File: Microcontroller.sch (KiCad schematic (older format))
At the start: 41 parts, among them CN2 CONN_RCPT_USB2.0_MINI_B_SMD_R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, M1 2N7002BK, M2 2N7002BK, Q10 2N7002BK, U2 STM32L412R8T6, X1 ABM3B-16.000MHZ

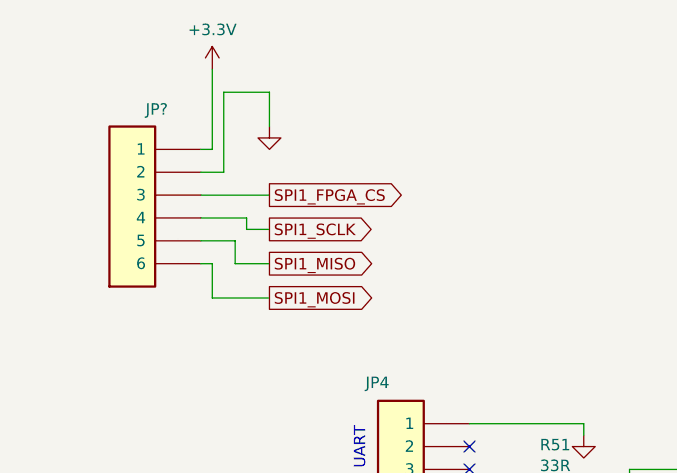
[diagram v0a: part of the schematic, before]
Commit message: Moved UART off FPGA bank 1, attached PB signals to FPGA
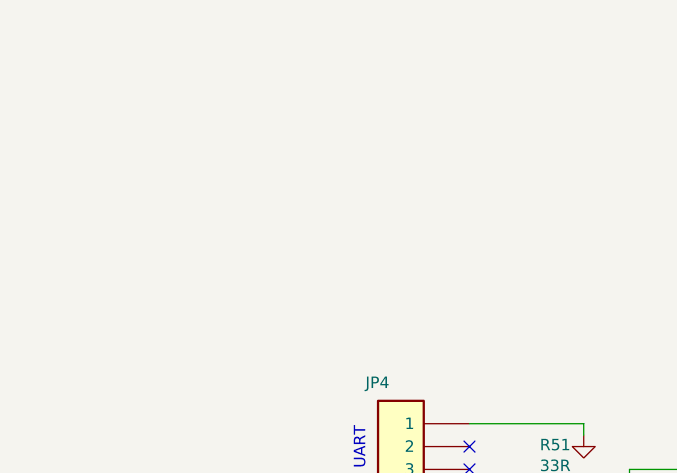
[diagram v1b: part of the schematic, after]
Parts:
- removed JP?: Pin_Header,_1x6-Way,_2.54mm_Pitch, symbol OpenVent:Pin_Header,_1x6-Way,_2.54mm_Pitch
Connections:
- wire segments 197 -> 181
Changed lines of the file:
@@
 Text Notes 8250 4150 0    50   ~ 0
 nRESET leftover from SWD,\nto be replaced with JTAG nRST\nsignal. LM 09/03/21
-$Comp
-L OpenVent:Pin_Header,_1x6-Way,_2.54mm_Pitch JP?
-U 1 1 6050B782
-P 1200 1700
-F 0 "JP?" H 1393 2375 50  0000 C CNN
-F 1 "Pin_Header,_1x6-Way,_2.54mm_Pitch" H 1400 2200 50  0001 C CNN
-F 2 "" H 1400 2200 50  0001 C CNN
-F 3 "" H 1400 2200 50  0001 C CNN
-	1    1200 1700
-	-1   0    0    -1
-$EndComp
-$Comp
-L OpenVent:+3.3V #PWR?
-U 1 1 6050E8FB
-P 1250 850
-F 0 "#PWR?" H 1250 700 50  0001 C CNN
-F 1 "+3.3V" H 1250 1023 50  0000 C CNN
-F 2 "" H 1250 850 50  0001 C CNN
-F 3 "" H 1250 850 50  0001 C CNN
-	1    1250 850
-	1    0    0    -1
-$EndComp
-$Comp
-L OpenVent:GND #PWR?
-U 1 1 6050F327
-P 1500 1100
-F 0 "#PWR?" H 1500 850 50  0001 C CNN
-F 1 "GND" H 1500 950 50  0001 C CNN
-F 2 "" H 1500 1100 50  0001 C CNN
-F 3 "" H 1500 1100 50  0001 C CNN
-	1    1500 1100
-	1    0    0    -1
-$EndComp
-Text GLabel 1500 1400 2    50   Output ~ 0
-SPI1_FPGA_CS
-Text GLabel 1500 1700 2    50   Output ~ 0
-SPI1_MISO
-Text GLabel 1500 1850 2    50   Output ~ 0
-SPI1_MOSI
-Text GLabel 1500 1550 2    50   Output ~ 0
-SPI1_SCLK
-Wire Wire Line
-	1200 1200 1250 1200
-Wire Wire Line
-	1250 1200 1250 850
-Wire Wire Line
-	1200 1300 1300 1300
-Wire Wire Line
-	1300 1300 1300 950
-Wire Wire Line
-	1300 950  1500 950
-Wire Wire Line
-	1500 950  1500 1100
-Wire Wire Line
-	1200 1400 1500 1400
-Wire Wire Line
-	1200 1500 1400 1500
-Wire Wire Line
-	1400 1500 1400 1550
-Wire Wire Line
-	1400 1550 1500 1550
-Wire Wire Line
-	1200 1600 1350 1600
-Wire Wire Line
-	1350 1600 1350 1700
-Wire Wire Line
-	1350 1700 1500 1700
-Wire Wire Line
-	1200 1700 1250 1700
-Wire Wire Line
-	1250 1700 1250 1850
-Wire Wire Line
-	1250 1850 1500 1850
 $EndSCHEMATC

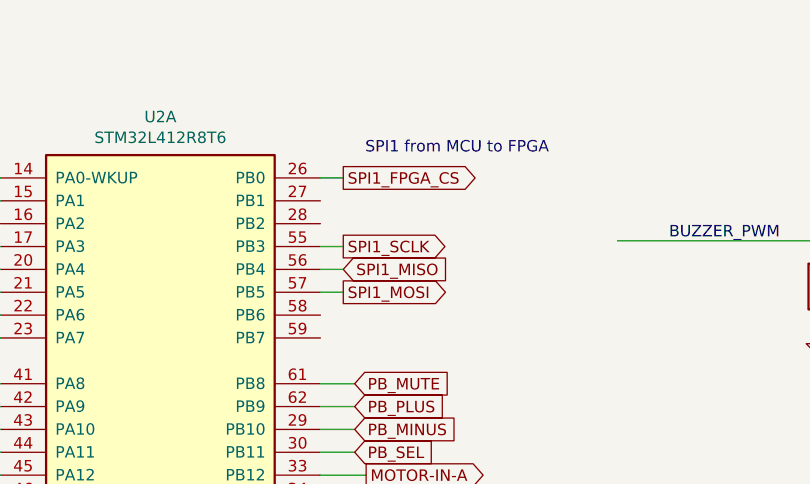
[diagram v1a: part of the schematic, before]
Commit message: Added FPGA_READY interrupt signal from FPGA to MCU
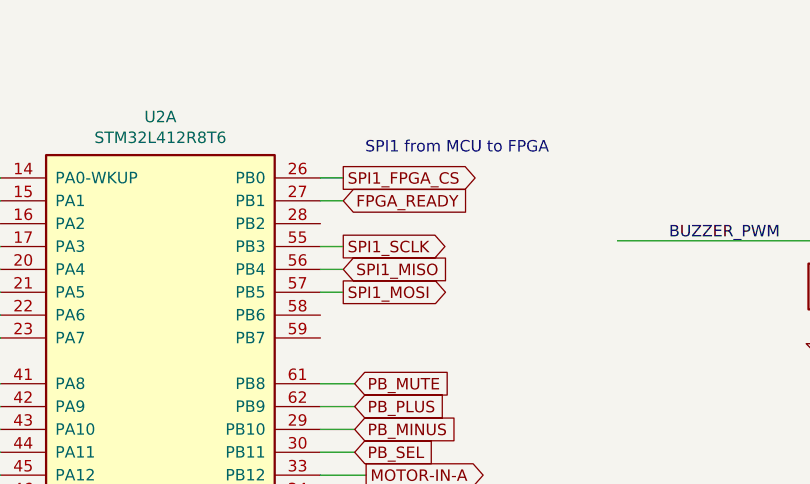
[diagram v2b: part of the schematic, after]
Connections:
- net labels added: FPGA_READY
- wire segments 181 -> 182
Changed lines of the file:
@@
 Text Notes 8250 4150 0    50   ~ 0
 nRESET leftover from SWD,\nto be replaced with JTAG nRST\nsignal. LM 09/03/21
+Text GLabel 6450 1700 2    50   Input ~ 0
+FPGA_READY
+Wire Wire Line
+	6350 1700 6450 1700
 $EndSCHEMATC

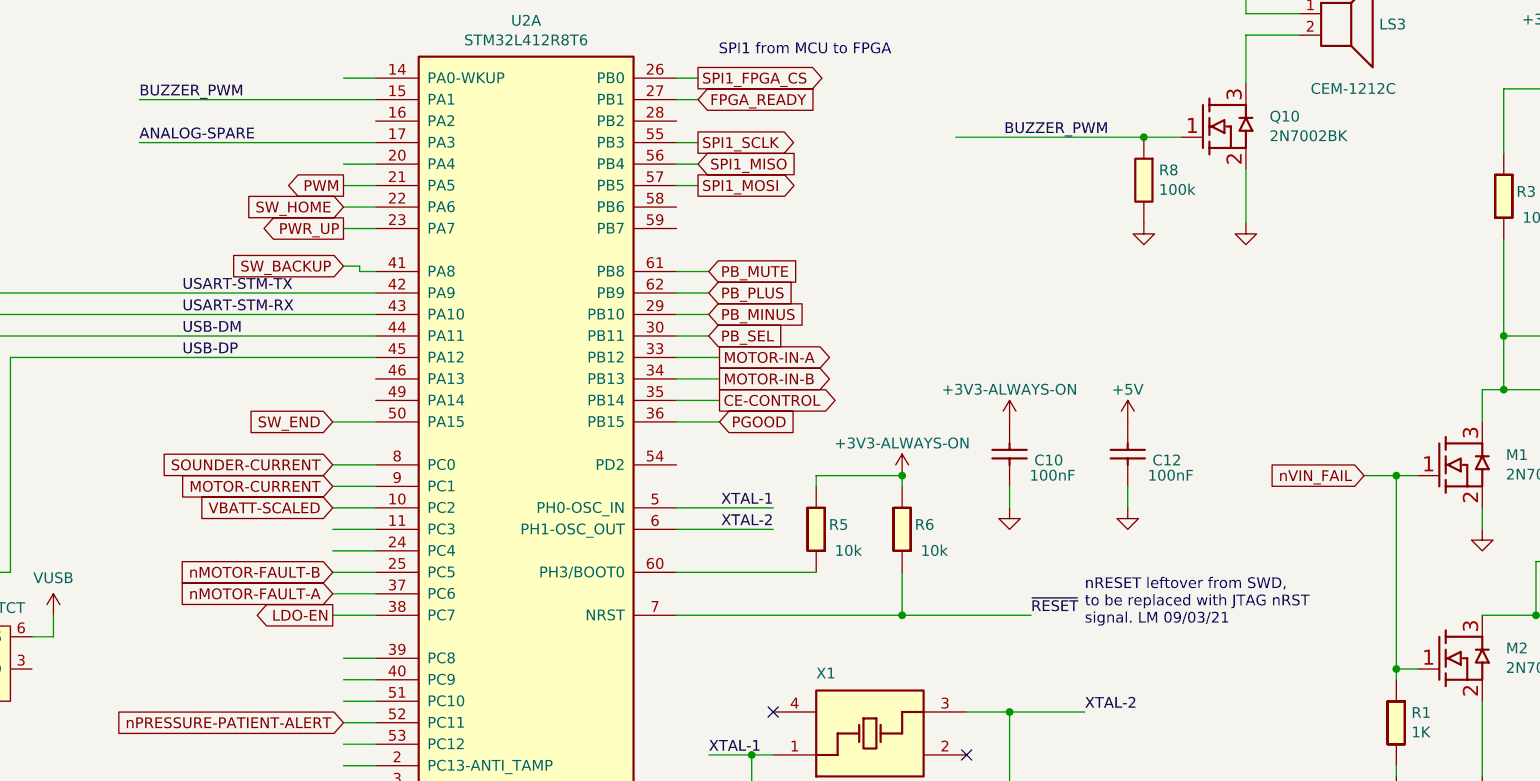
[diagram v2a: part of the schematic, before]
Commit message: JTAG pins were connected to the MCU
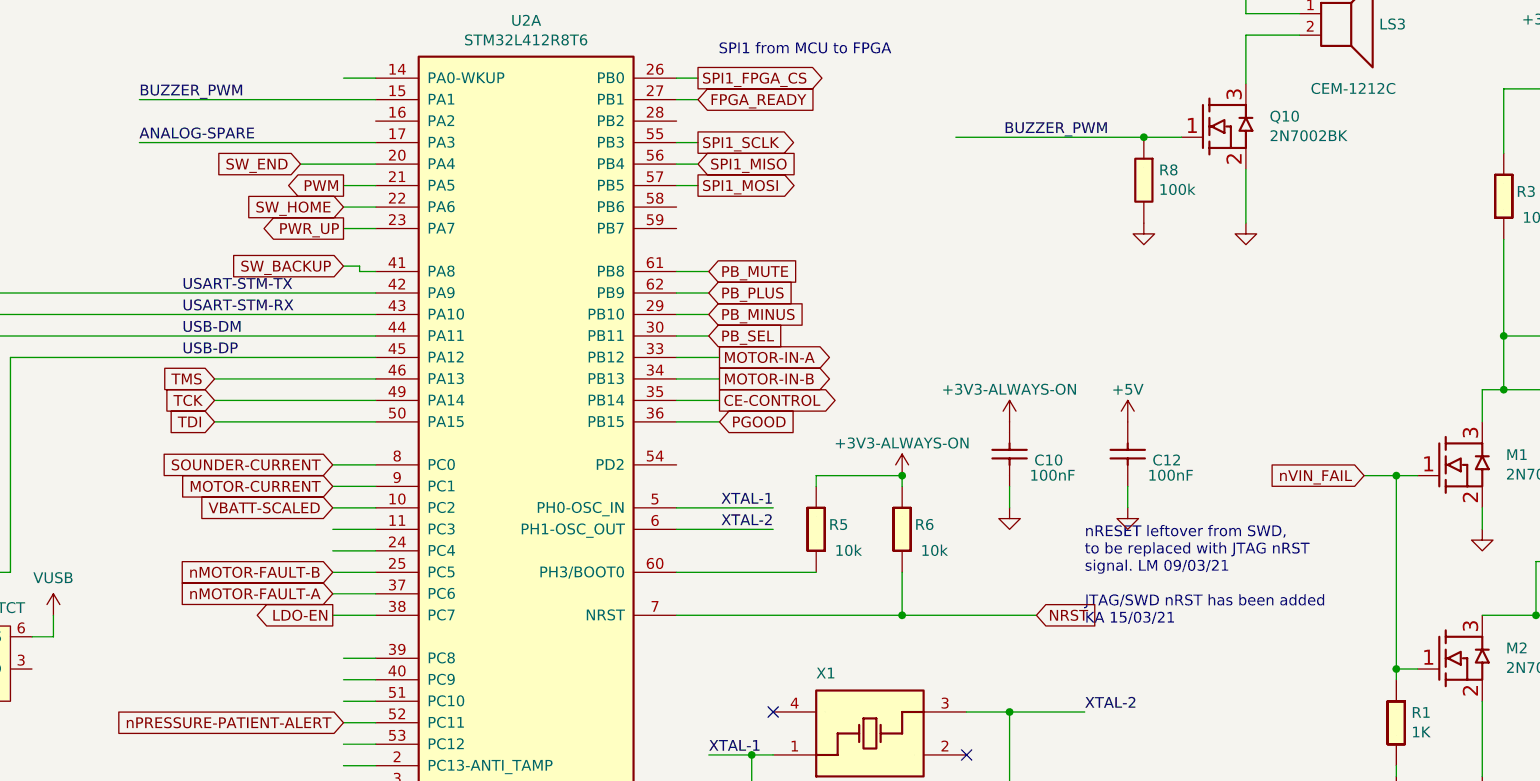
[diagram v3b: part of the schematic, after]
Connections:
- net labels added: NRST, TCK, TDI, TMS
- net labels removed: ~RESET~
- wire segments 182 -> 184
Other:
- note added: "nRESET leftover from SWD,\nto be replaced with JTAG nRST\nsignal. LM 09/03/21\n\nJTAG/SWD nRST has been added \nKA 15/03/21\n"
- note removed: "nRESET leftover from SWD,\nto be replaced with JTAG nRST\nsignal. LM 09/03/21"
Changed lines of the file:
@@
 	1    0    0    -1
 $EndComp
-Text Label 8000 4100 0    50   ~ 0
-~RESET~
 $Comp
 L OpenVent:GND #GND_09
@@
 	7400 3900 7400 4100
 Wire Wire Line
-	7400 4100 8000 4100
-Wire Wire Line
-	6350 4100 7400 4100
-Wire Wire Line
 	3575 6325 3575 6425
 Wire Wire Line
@@
 Connection ~ 3975 7025
 Connection ~ 4825 7025
-Connection ~ 7400 4100
 Connection ~ 7900 4550
 $Comp
@@
 	4750 4100 4950 4100
 Wire Wire Line
-	4800 2000 4950 2000
-Wire Wire Line
 	4800 2100 4950 2100
 Wire Wire Line
@@
 Text GLabel 4800 2475 0    50   Input ~ 0
 SW_BACKUP
-Text GLabel 4750 3200 0    50   Input ~ 0
+Text GLabel 4600 2000 0    50   Input ~ 0
 SW_END
-Wire Wire Line
-	4950 3200 4750 3200
 Wire Wire Line
 	4950 2200 4800 2200
@@
 $EndComp
 Text Notes 8250 4150 0    50   ~ 0
-nRESET leftover from SWD,\nto be replaced with JTAG nRST\nsignal. LM 09/03/21
+nRESET leftover from SWD,\nto be replaced with JTAG nRST\nsignal. LM 09/03/21\n\nJTAG/SWD nRST has been added \nKA 15/03/21\n
 Text GLabel 6450 1700 2    50   Input ~ 0
 FPGA_READY
 Wire Wire Line
 	6350 1700 6450 1700
+Wire Wire Line
+	4600 2000 4950 2000
+Text GLabel 4200 3000 0    50   Input ~ 0
+TMS
+Wire Wire Line
+	4200 3000 4950 3000
+Text GLabel 4200 3100 0    50   Input ~ 0
+TCK
+Wire Wire Line
+	4200 3100 4950 3100
+Text GLabel 4200 3200 0    50   Input ~ 0
+TDI
+Wire Wire Line
+	4200 3200 4950 3200
+Wire Wire Line
+	6350 4100 7400 4100
+Wire Wire Line
+	7400 4100 8025 4100
+Text GLabel 8025 4100 2    50   Input ~ 0
+NRST
+Connection ~ 7400 4100
 $EndSCHEMATC

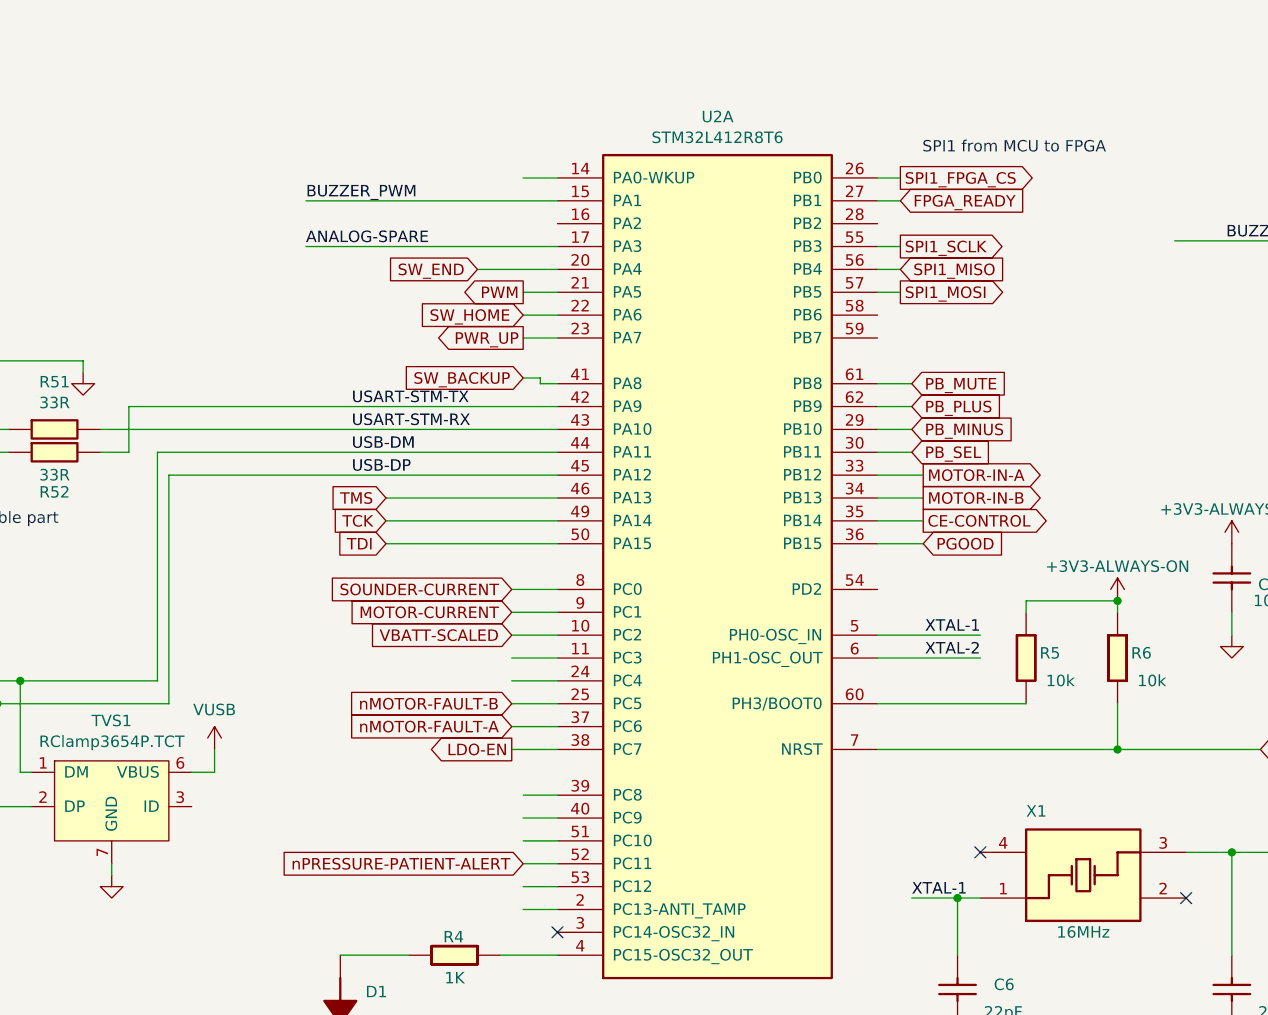
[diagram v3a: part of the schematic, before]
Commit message: Changed which pins SPI1 go into MCU on to allow for JTAG connection
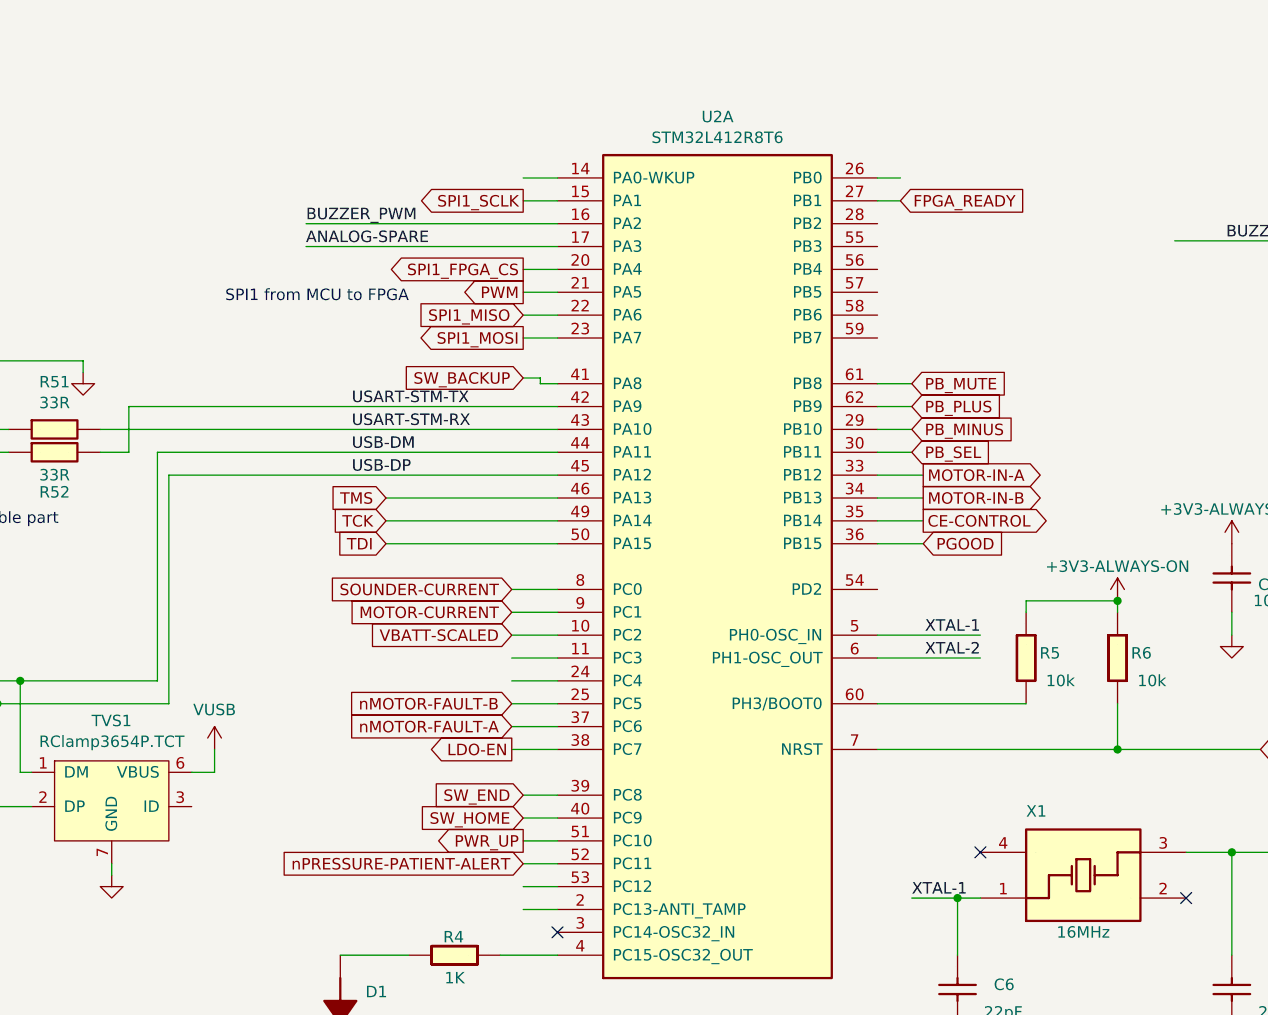
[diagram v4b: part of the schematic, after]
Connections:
- wire segments 184 -> 182
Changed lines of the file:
@@
 	1    0    0    -1
 $EndComp
-Text GLabel 4800 2300 0    50   Output ~ 0
+Text GLabel 4800 4500 0    50   Output ~ 0
 PWR_UP
 $Comp
@@
 Text GLabel 4800 2475 0    50   Input ~ 0
 SW_BACKUP
-Text GLabel 4600 2000 0    50   Input ~ 0
+Text GLabel 4800 4300 0    50   Input ~ 0
 SW_END
 Wire Wire Line
@@
 Wire Wire Line
 	4875 2475 4800 2475
-Text GLabel 6450 1600 2    50   Output ~ 0
+Text GLabel 4800 2000 0    50   Output ~ 0
 SPI1_FPGA_CS
-Text GLabel 6450 1900 2    50   Output ~ 0
+Text GLabel 4800 1700 0    50   Output ~ 0
 SPI1_SCLK
-Text GLabel 6450 2000 2    50   Input ~ 0
-SPI1_MISO
-Text GLabel 6450 2100 2    50   Output ~ 0
-SPI1_MOSI
 Wire Wire Line
 	6350 1600 6450 1600
-Wire Wire Line
-	6350 1900 6450 1900
-Wire Wire Line
-	6350 2000 6450 2000
-Wire Wire Line
-	6350 2100 6450 2100
-Text Notes 7350 1500 2    50   ~ 0
+Text Notes 4300 2150 2    50   ~ 0
 SPI1 from MCU to FPGA
-Text GLabel 4800 2200 0    50   Input ~ 0
+Text GLabel 4800 4400 0    50   Input ~ 0
 SW_HOME
 $Comp
@@
 	7650 1875 8525 1875
 Wire Wire Line
-	3850 1700 4950 1700
-Text Label 3850 1700 0    50   ~ 0
+	3850 1800 4950 1800
+Text Label 3850 1800 0    50   ~ 0
 BUZZER_PWM
 Text GLabel 6500 2500 2    50   Input ~ 0
@@
 Wire Wire Line
 	6350 1700 6450 1700
-Wire Wire Line
-	4600 2000 4950 2000
 Text GLabel 4200 3000 0    50   Input ~ 0
 TMS
@@
 NRST
 Connection ~ 7400 4100
+Wire Wire Line
+	4950 1700 4800 1700
+Wire Wire Line
+	4800 2000 4950 2000
+Text GLabel 4800 2300 0    50   Output ~ 0
+SPI1_MOSI
+Text GLabel 4800 2200 0    50   Input ~ 0
+SPI1_MISO
 $EndSCHEMATC

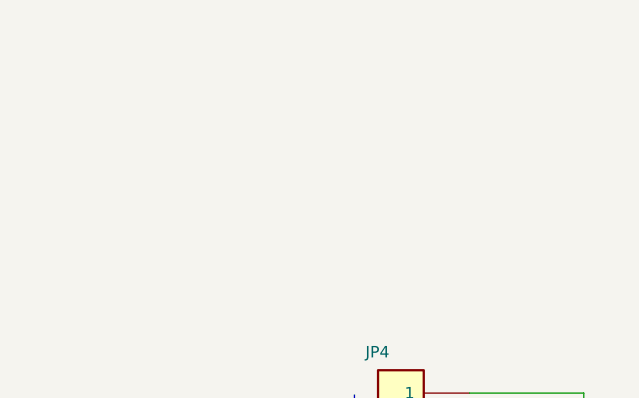
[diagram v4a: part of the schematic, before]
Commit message: Logic Analyser connector added for MCU SPI and FPGA_READY signals
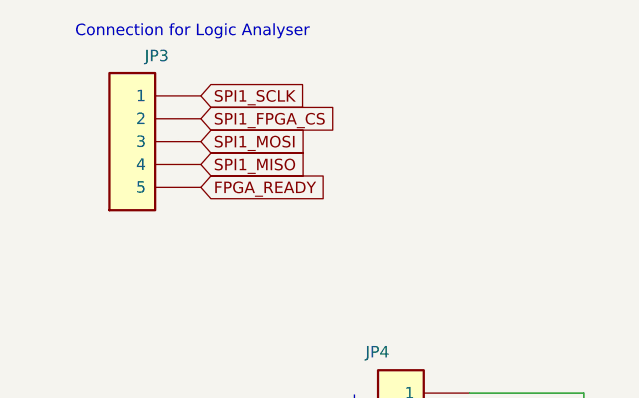
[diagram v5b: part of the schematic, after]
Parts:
- added JP3: Pin_Header,_1x5-Way,_2.54mm_Pitch, symbol OpenVent:Pin_Header,_1x5-Way,_2.54mm_Pitch
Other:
- note added: "Connection for Logic Analyser"
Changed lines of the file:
@@
 Text GLabel 4800 2200 0    50   Input ~ 0
 SPI1_MISO
+$Comp
+L OpenVent:Pin_Header,_1x5-Way,_2.54mm_Pitch JP3
+U 1 1 6063147A
+P 1200 1500
+F 0 "JP3" H 1393 2075 50  0000 C CNN
+F 1 "Pin_Header,_1x5-Way,_2.54mm_Pitch" H 1400 1900 50  0001 C CNN
+F 2 "" H 1400 1900 50  0001 C CNN
+F 3 "" H 1400 1900 50  0001 C CNN
+	1    1200 1500
+	-1   0    0    -1
+$EndComp
+Text Notes 650  850  0    50   ~ 0
+Connection for Logic Analyser
+Text GLabel 1200 1100 2    50   Input ~ 0
+SPI1_SCLK
+Text GLabel 1200 1200 2    50   Input ~ 0
+SPI1_FPGA_CS
+Text GLabel 1200 1300 2    50   Input ~ 0
+SPI1_MOSI
+Text GLabel 1200 1400 2    50   Input ~ 0
+SPI1_MISO
+Text GLabel 1200 1500 2    50   Input ~ 0
+FPGA_READY
 $EndSCHEMATC
